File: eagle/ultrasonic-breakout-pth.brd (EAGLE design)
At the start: 100 x 80 mm, 25 parts, among them Q1 16 MHz, U1 ATMEGA328P_PDIP

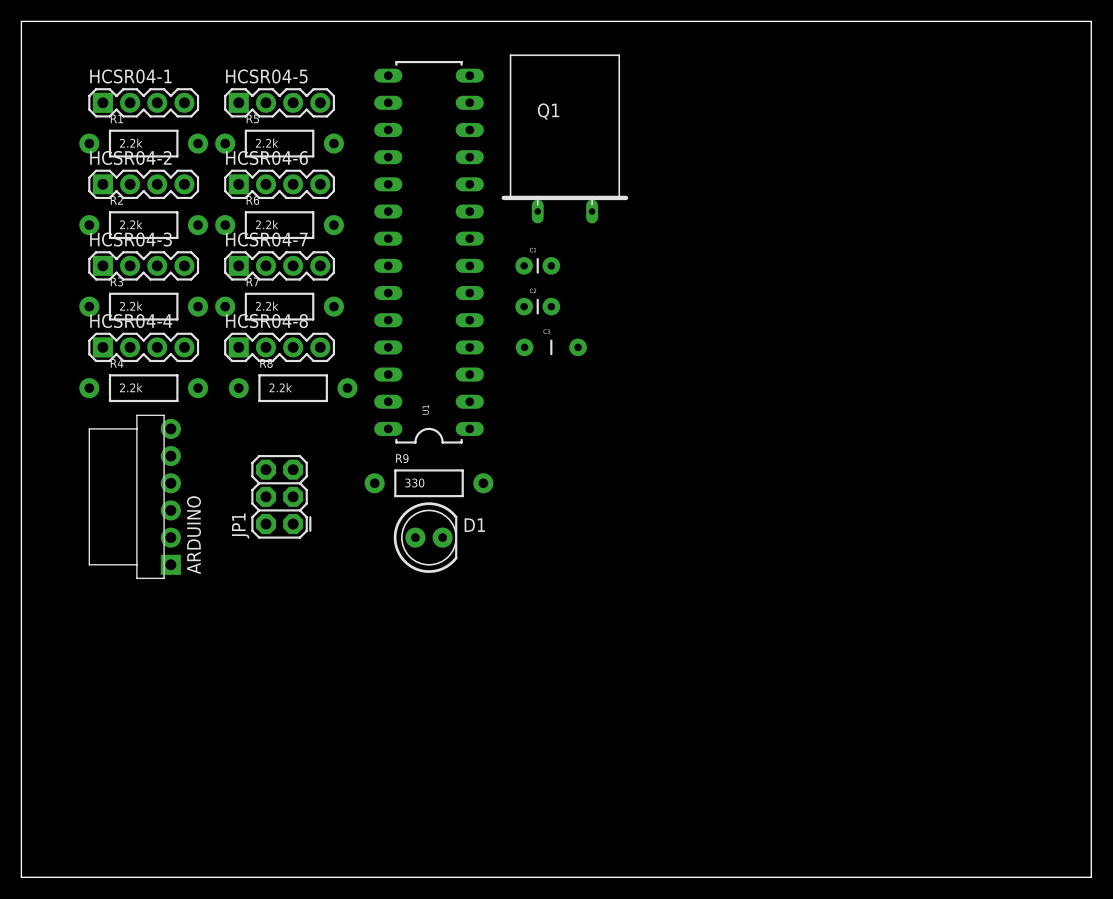
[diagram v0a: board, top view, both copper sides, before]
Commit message: improve board layout
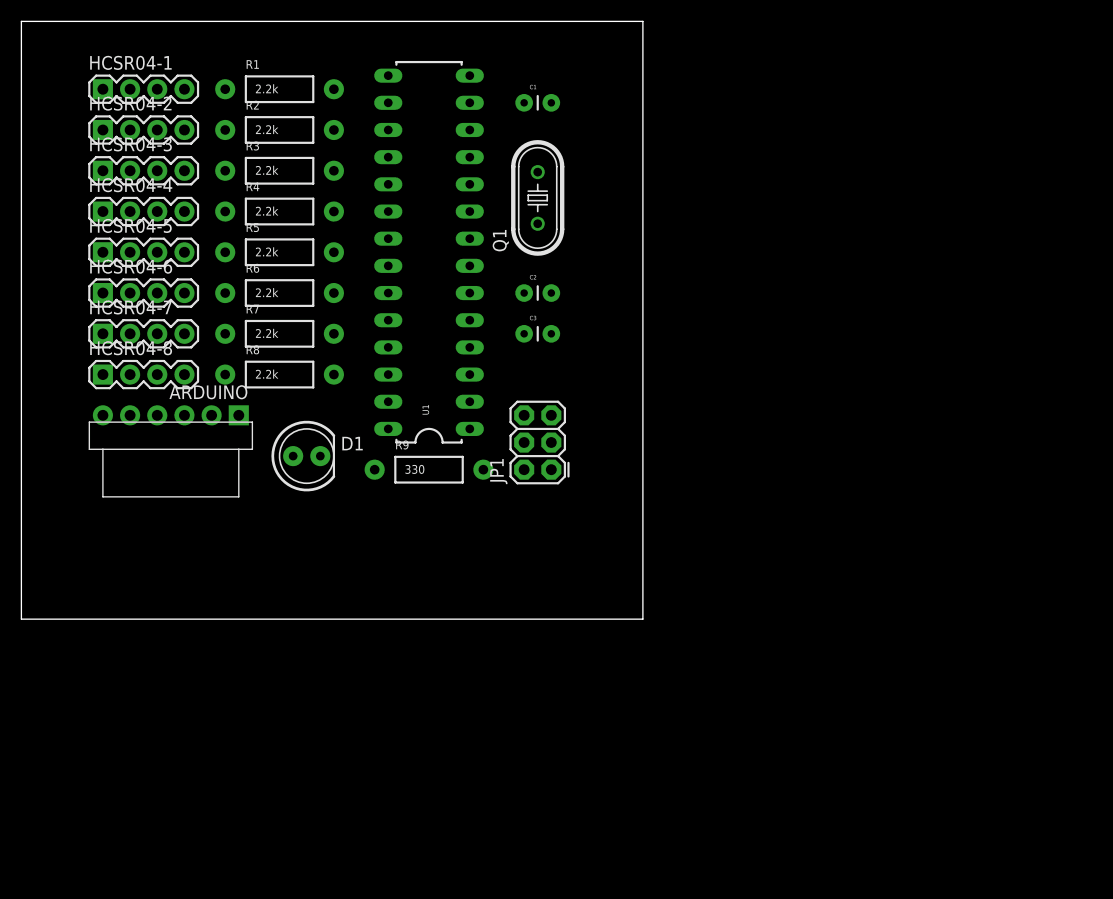
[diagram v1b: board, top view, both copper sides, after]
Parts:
- C3: device SparkFun-Passives:CAP-PTH-5MM -> SparkFun-Capacitors:CAP-PTH-SMALL
- Q1: device special:Q -> SparkFun-FreqCtrl:HC49U-V
- moved JP1 24.7 mm to (49.5, 38.1)
- moved R4 20.8 mm to (24.1, 62.2)
- moved HCSR04-5 18.9 mm to (7.62, 58.4)
- moved R3 18.0 mm to (24.1, 66.0)
- moved HCSR04-6 16.3 mm to (7.62, 54.6)
- moved R2 15.5 mm to (24.1, 69.8)
- moved ARDUINO 15.3 mm to (20.3, 43.2), turned to 180 degrees
- moved C1 15.2 mm to (47.0, 72.4)
- moved HCSR04-7 14.2 mm to (7.62, 50.8)
- moved D1 13.7 mm to (26.7, 39.4)
- moved R1 13.7 mm to (24.1, 73.7)
- moved HCSR04-8 13.0 mm to (7.62, 47.0)
- moved HCSR04-4 12.7 mm to (7.62, 62.2)
- moved R5 10.2 mm to (24.1, 58.4)
- moved HCSR04-3 8.89 mm to (7.62, 66.0)
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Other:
- board size 100 x 80 mm -> 58.1 x 55.9 mm

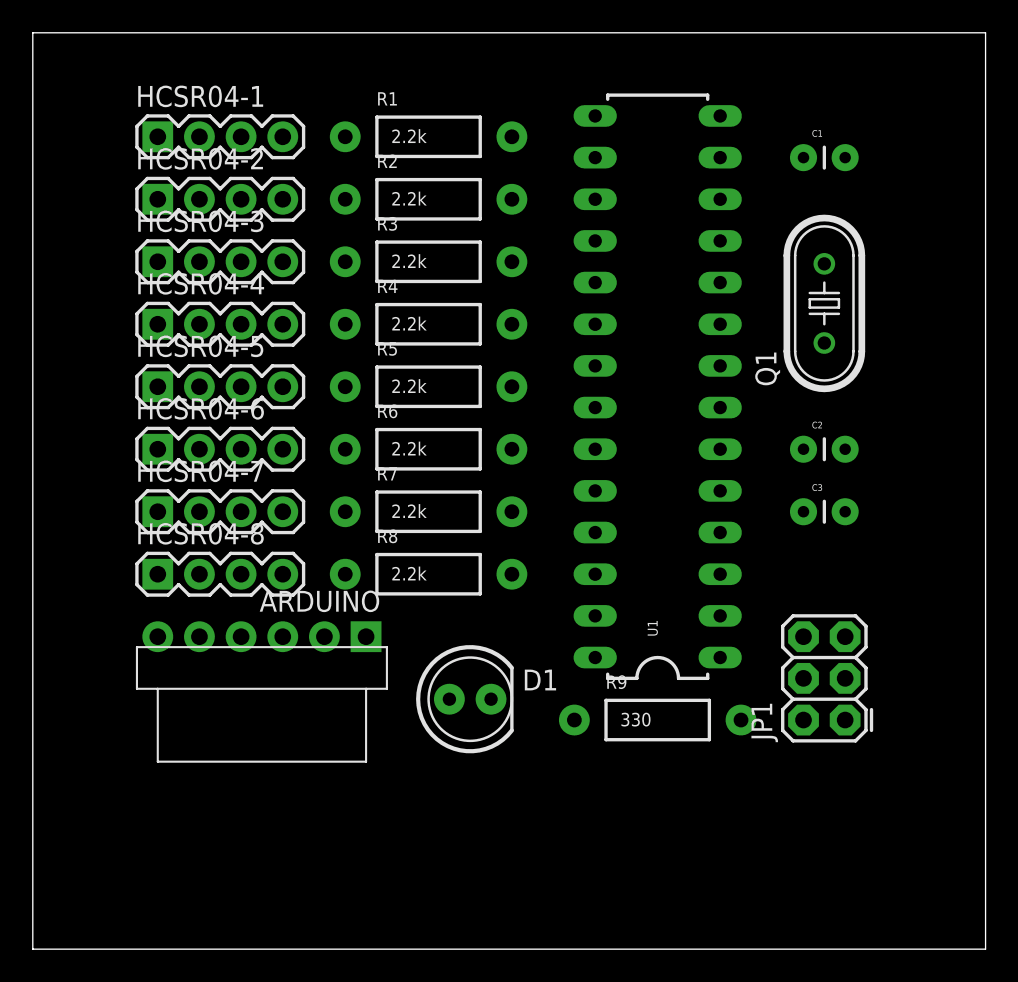
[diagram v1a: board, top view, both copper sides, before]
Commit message: improve board layout
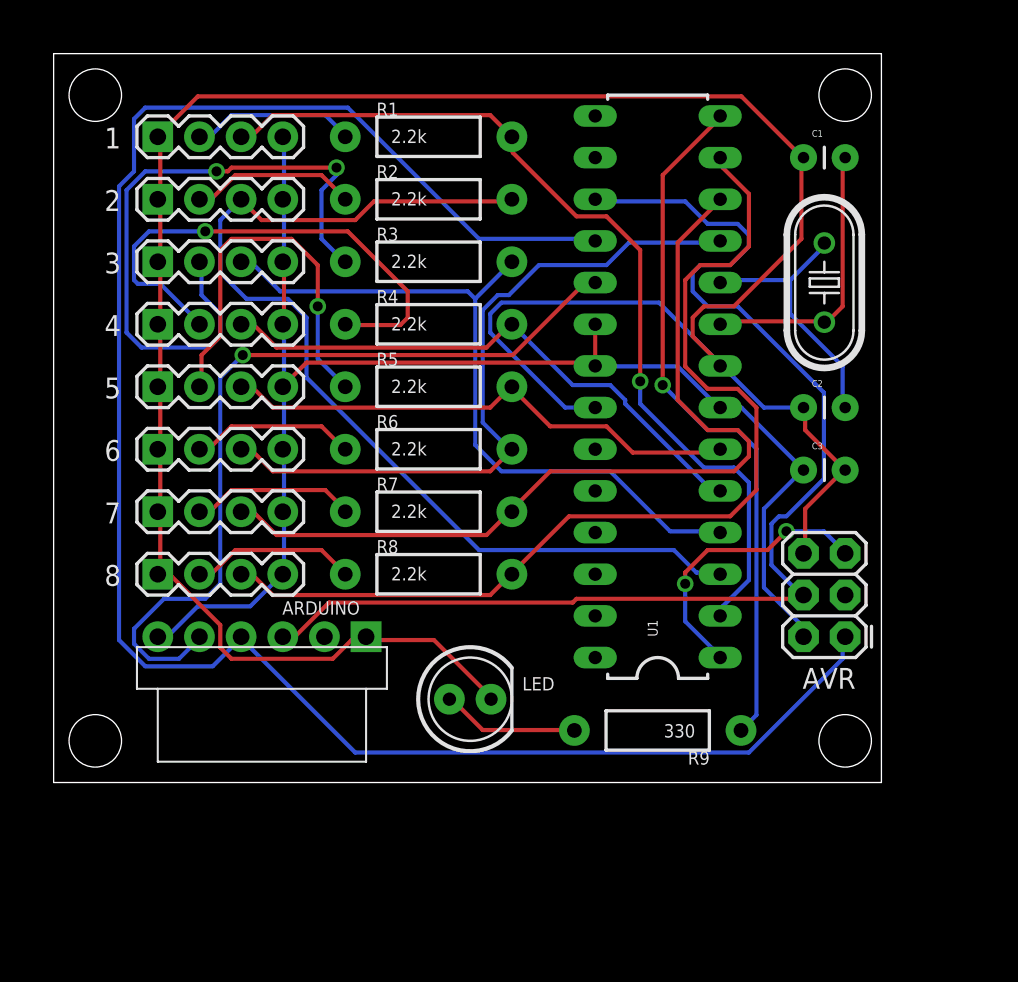
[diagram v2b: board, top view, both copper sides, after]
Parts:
- removed JP1: AVR_SPI_PRG_6PTH, SparkFun-Connectors:2X3
- added AVR: AVR_SPI_PRG_6PTH, SparkFun-Connectors:2X3
- moved C3 2.54 mm to (47.0, 53.3)
- moved C2 2.54 mm to (47.0, 57.1)
- moved Q1 1.27 mm to (48.3, 64.8)
- moved R9 0.63 mm to (38.1, 37.5), turned to 180 degrees
- renumbered D1 to LED, HCSR04-1 to 1, HCSR04-2 to 2, HCSR04-3 to 3, HCSR04-4 to 4, HCSR04-5 to 5, HCSR04-6 to 6, HCSR04-7 to 7, HCSR04-8 to 8
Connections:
- net N$4 renamed TRIGGER1
- net 5V: now also AVR.2; no longer JP1.2
- net GND: now also AVR.6; no longer JP1.6
- net MISO: now also AVR.1; no longer JP1.1
- net MOSI: now also AVR.4; no longer JP1.4
- net N$2: now also AVR.5; no longer JP1.5
- net SCK: now also AVR.3; no longer JP1.3
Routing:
- net GND: track 0.00 -> 155.2 mm
- net MISO: track 0.00 -> 116.3 mm
- net 5V: track 0.00 -> 86.1 mm
- net MOSI: track 0.00 -> 74.4 mm
- net PD1: track 0.00 -> 62.8 mm
- net PD7: track 0.00 -> 61.2 mm
- net PD0: track 0.00 -> 55.7 mm, vias 0 -> 1
- net PD6: track 0.00 -> 53.2 mm
- net SCK: track 0.00 -> 50.2 mm, vias 0 -> 1
- net PD2: track 0.00 -> 44.5 mm
- net PD5: track 0.00 -> 43.2 mm
- net N$12: track 0.00 -> 42.7 mm, vias 0 -> 1
- net N$6: track 0.00 -> 40.2 mm, vias 0 -> 2
- net PD3: track 0.00 -> 34.7 mm
- net PD4: track 0.00 -> 32.1 mm
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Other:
- board size 58.1 x 55.9 mm -> 50.5 x 44.4 mm
- board text added: "5V"
- board text added: "Copyright 2016 Grove Enterprises LLC"
- board text added: "Echo"
- board text added: "GND"
- board text added: "HC-SR04 Breakout 1.0"
- board text added: "Trig"

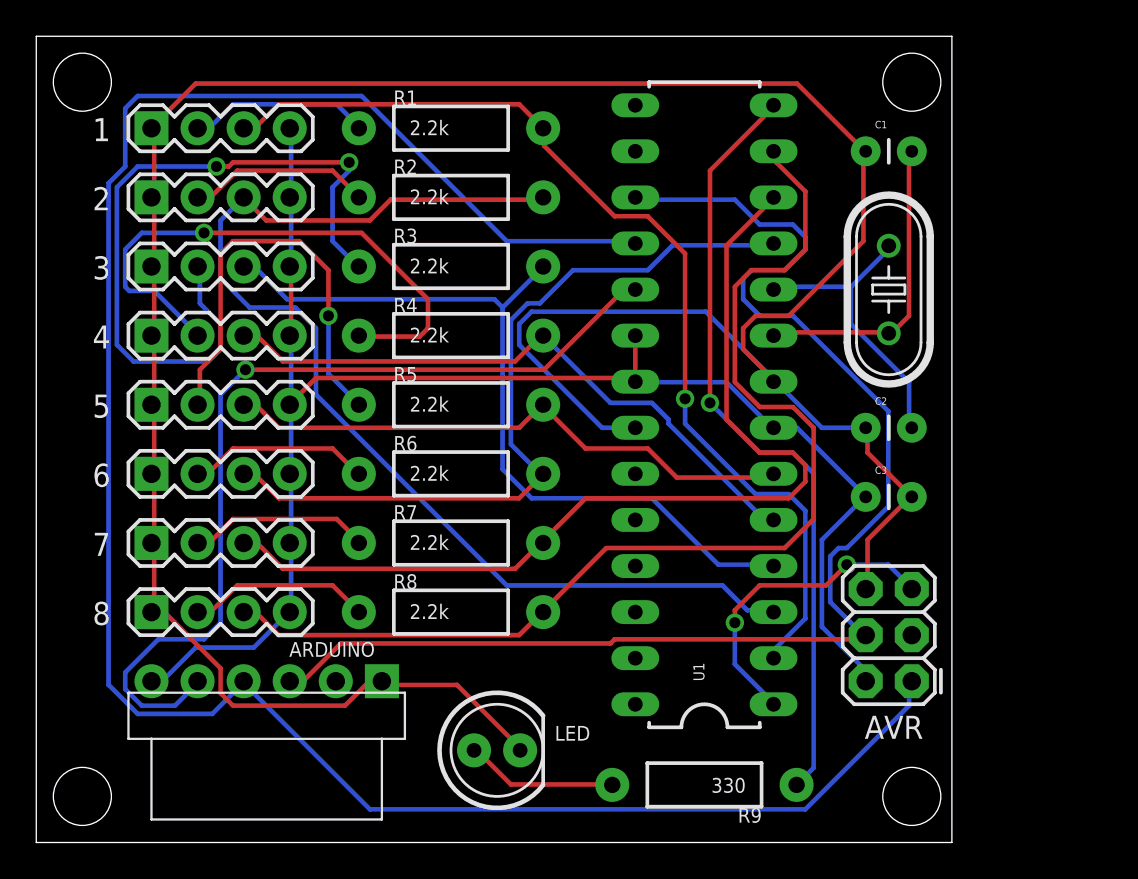
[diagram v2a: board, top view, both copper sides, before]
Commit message: improve board layout
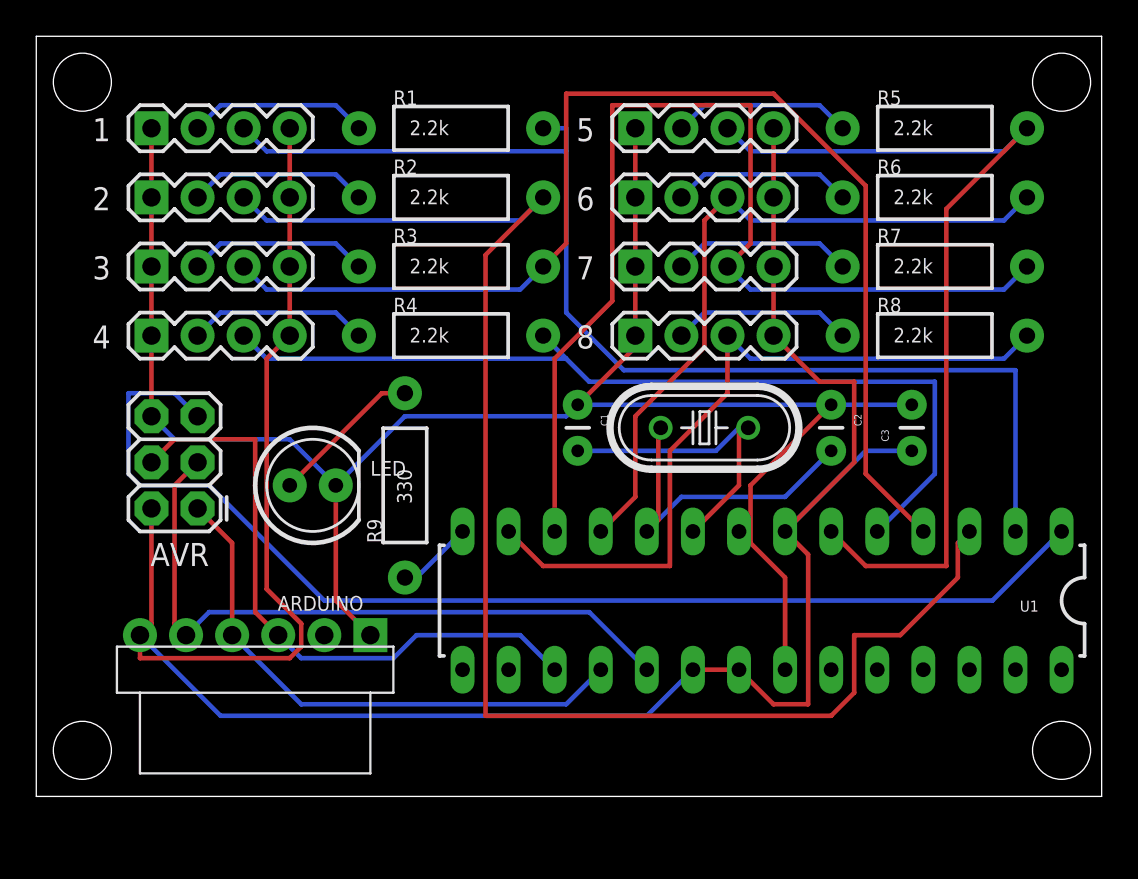
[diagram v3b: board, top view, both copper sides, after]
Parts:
- moved AVR 40.5 mm to (10.2, 52.7)
- moved 7 30.7 mm to (34.3, 66.0)
- moved R7 30.7 mm to (50.8, 66.0)
- moved 5 30.7 mm to (34.3, 73.7)
- moved 6 30.7 mm to (34.3, 69.8)
- moved 8 30.7 mm to (34.3, 62.2)
- moved R5 30.7 mm to (50.8, 73.7)
- moved R6 30.7 mm to (50.8, 69.8)
- moved R8 30.7 mm to (50.8, 62.2)
- moved R9 23.3 mm to (21.6, 54.0), turned to 90 degrees
- moved C1 21.1 mm to (31.1, 58.4), turned to 270 degrees
- moved LED 17.8 mm to (16.5, 54.0)
- moved Q1 12.7 mm to (38.1, 57.1), turned to 180 degrees
- moved U1 11.3 mm to (41.3, 47.6), turned to 180 degrees
- moved C3 3.59 mm to (49.5, 55.9), turned to 90 degrees
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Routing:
- net MISO: track 116.3 -> 30.5 mm
- net GND: track 155.2 -> 104.9 mm
- net 5V: track 86.1 -> 133.7 mm
- net N$2: track 17.4 -> 64.7 mm, vias 2 -> 0
- net MOSI: track 74.4 -> 34.6 mm
- net N$12: track 42.7 -> 4.23 mm, vias 1 -> 0
- net N$6: track 40.2 -> 9.94 mm, vias 2 -> 0
- net PD2: track 44.5 -> 66.6 mm
- net N$7: track 31.4 -> 9.94 mm, vias 1 -> 0
- net PD7: track 61.2 -> 41.3 mm
- net PD4: track 32.1 -> 50.7 mm
- net PD1: track 62.8 -> 81.3 mm
- net PD3: track 34.7 -> 50.5 mm
- net N$8: track 23.9 -> 9.94 mm, vias 1 -> 0
- net SCK: track 50.2 -> 37.6 mm, vias 1 -> 0
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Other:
- board size 50.5 x 44.4 mm -> 58.7 x 41.9 mm

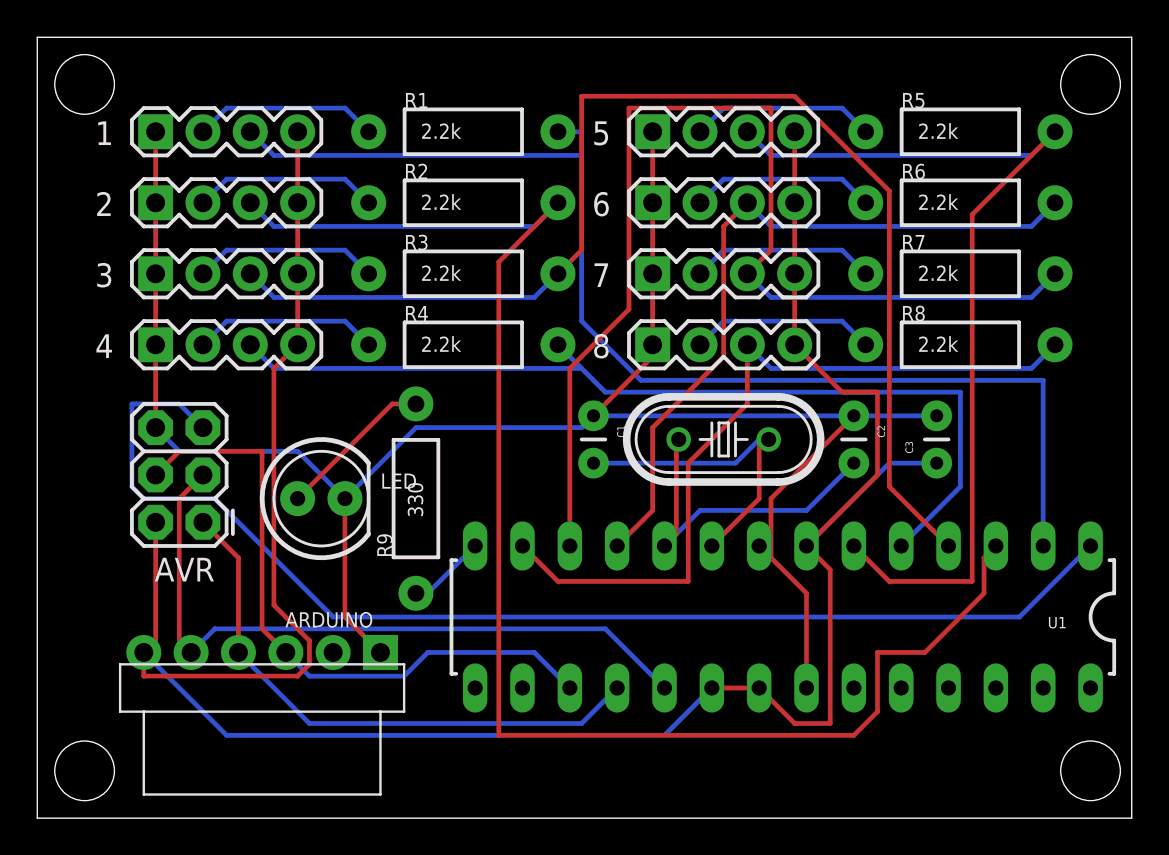
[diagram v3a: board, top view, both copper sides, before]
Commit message: fixed missing SS connection in schematic, also switched to 5mm capacitor and completely redesigned board layout
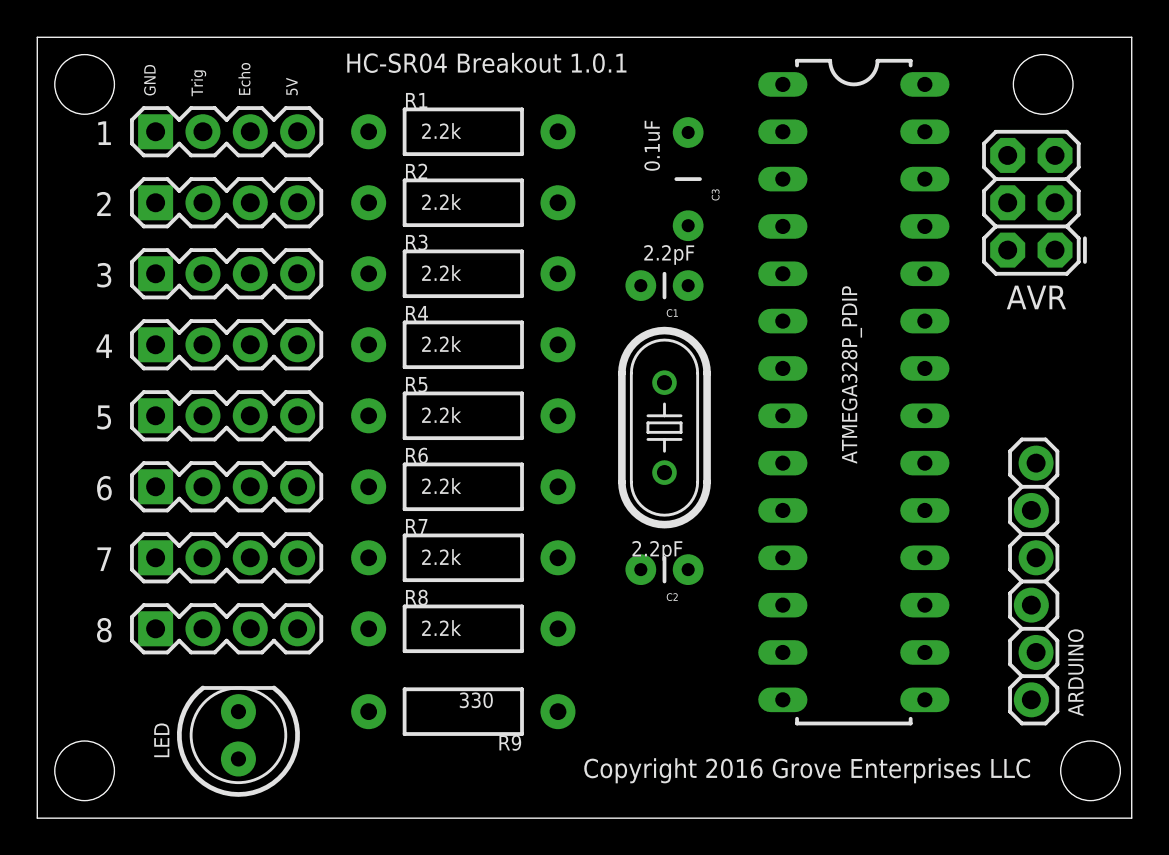
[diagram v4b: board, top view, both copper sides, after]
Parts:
- ARDUINO: device SparkFun-Connectors:MOLEX-1X6-RA -> SparkFun-Connectors:1X06_LOCK
- C3: device SparkFun-Capacitors:CAP-PTH-SMALL -> SparkFun-Capacitors:CAP-PTH-5MM
- moved AVR 48.0 mm to (55.9, 67.3)
- moved ARDUINO 35.0 mm to (54.6, 43.2), turned to 90 degrees
- moved 7 30.7 mm to (7.62, 50.8)
- moved R7 30.7 mm to (24.1, 50.8)
- moved 5 30.7 mm to (7.62, 58.4)
- moved 6 30.7 mm to (7.62, 54.6)
- moved 8 30.7 mm to (7.62, 47.0)
- moved R5 30.7 mm to (24.1, 58.4)
- moved R6 30.7 mm to (24.1, 54.6)
- moved R8 30.7 mm to (24.1, 47.0)
- moved C3 20.3 mm to (36.2, 71.1), turned to 270 degrees
- moved LED 13.5 mm to (12.1, 41.3), turned to 90 degrees
- moved U1 12.7 mm to (45.1, 59.7), turned to 270 degrees
- moved C2 12.1 mm to (36.2, 50.2), turned to 180 degrees
- moved R9 11.7 mm to (24.1, 42.5), turned to 180 degrees
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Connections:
- net SS: now also U1.16
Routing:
- net 5V: track 133.7 -> 0.00 mm
- net GND: track 104.9 -> 0.00 mm
- net PD1: track 81.3 -> 0.00 mm
- net PD2: track 66.6 -> 0.00 mm
- net PD0: track 64.7 -> 0.00 mm
- net N$2: track 64.7 -> 0.00 mm
- net PD6: track 59.4 -> 0.00 mm
- net PD4: track 50.7 -> 0.00 mm
- net PD3: track 50.5 -> 0.00 mm
- net PD7: track 41.3 -> 0.00 mm
- net PD5: track 38.9 -> 0.00 mm
- net SCK: track 37.6 -> 0.00 mm
- net MOSI: track 34.6 -> 0.00 mm
- net MISO: track 30.5 -> 0.00 mm
- net N$3: track 18.1 -> 0.00 mm
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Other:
- board text added: "HC-SR04 Breakout 1.0.1"
- board text removed: "HC-SR04 Breakout 1.0"
